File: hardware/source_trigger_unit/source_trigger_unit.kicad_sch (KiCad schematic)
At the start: 12 parts, among them J1 SMA, J2 SMA, J3 BANANA, 4mm, P1 IEC_60320_C13_Plug, SW1 SW_Nidec_CAS-120A1

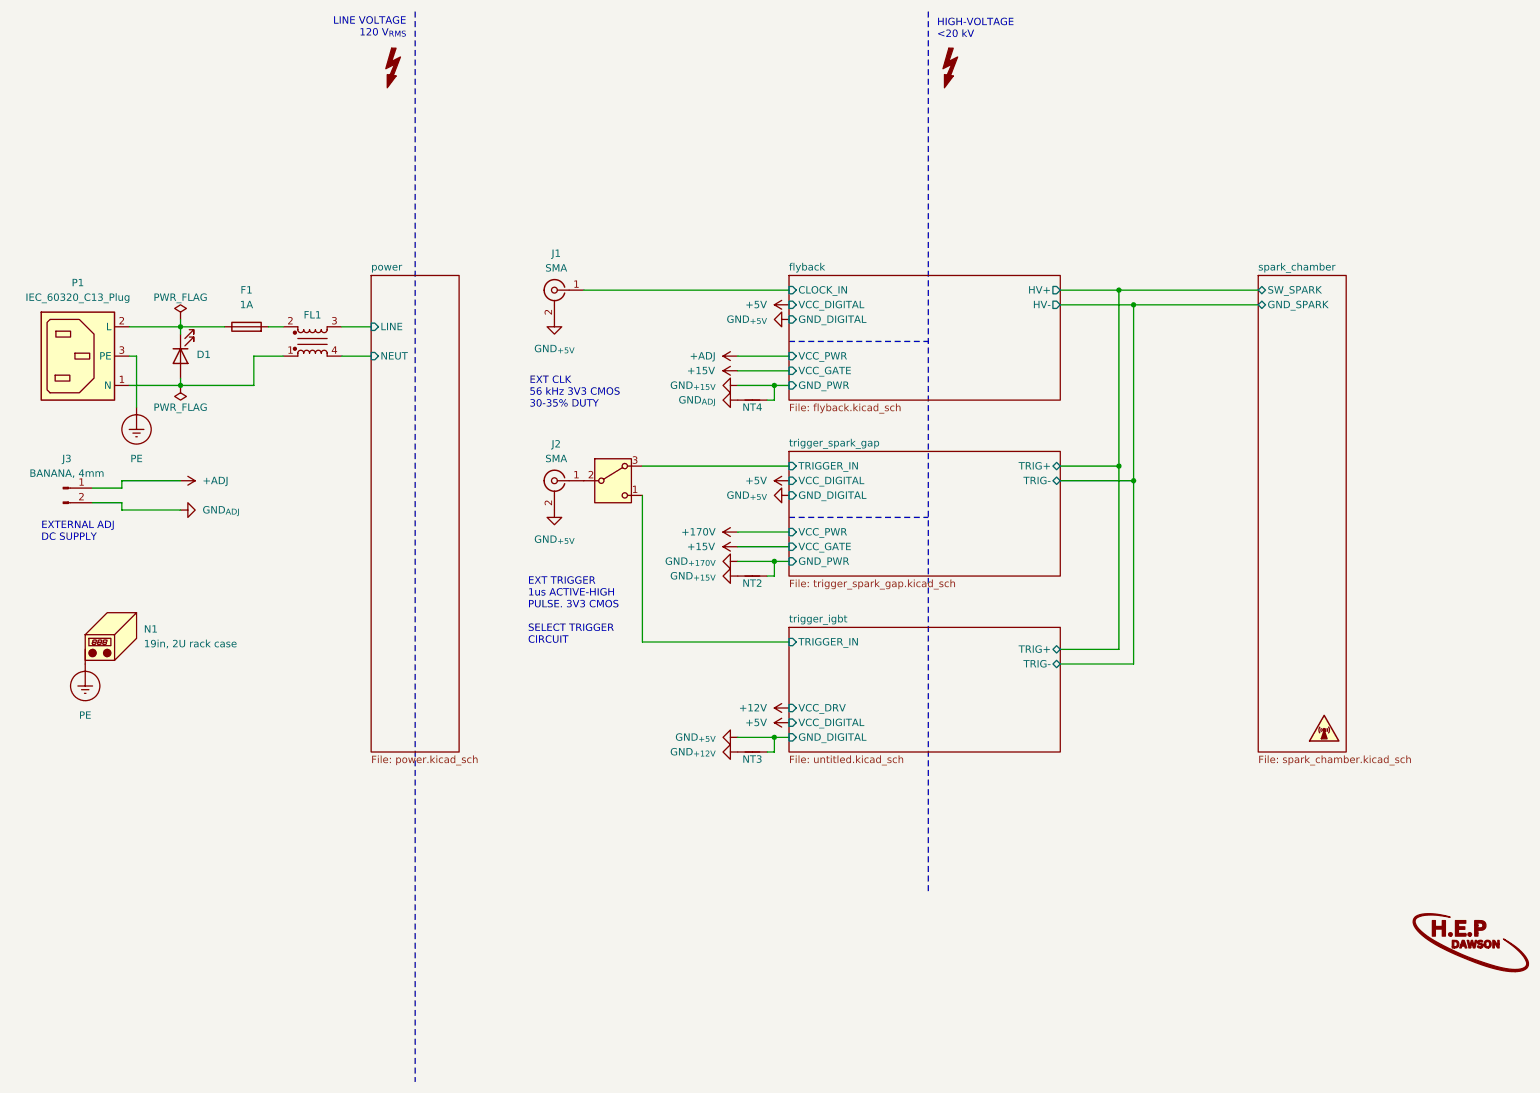
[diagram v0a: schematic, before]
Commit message: add titles & reformat schematics
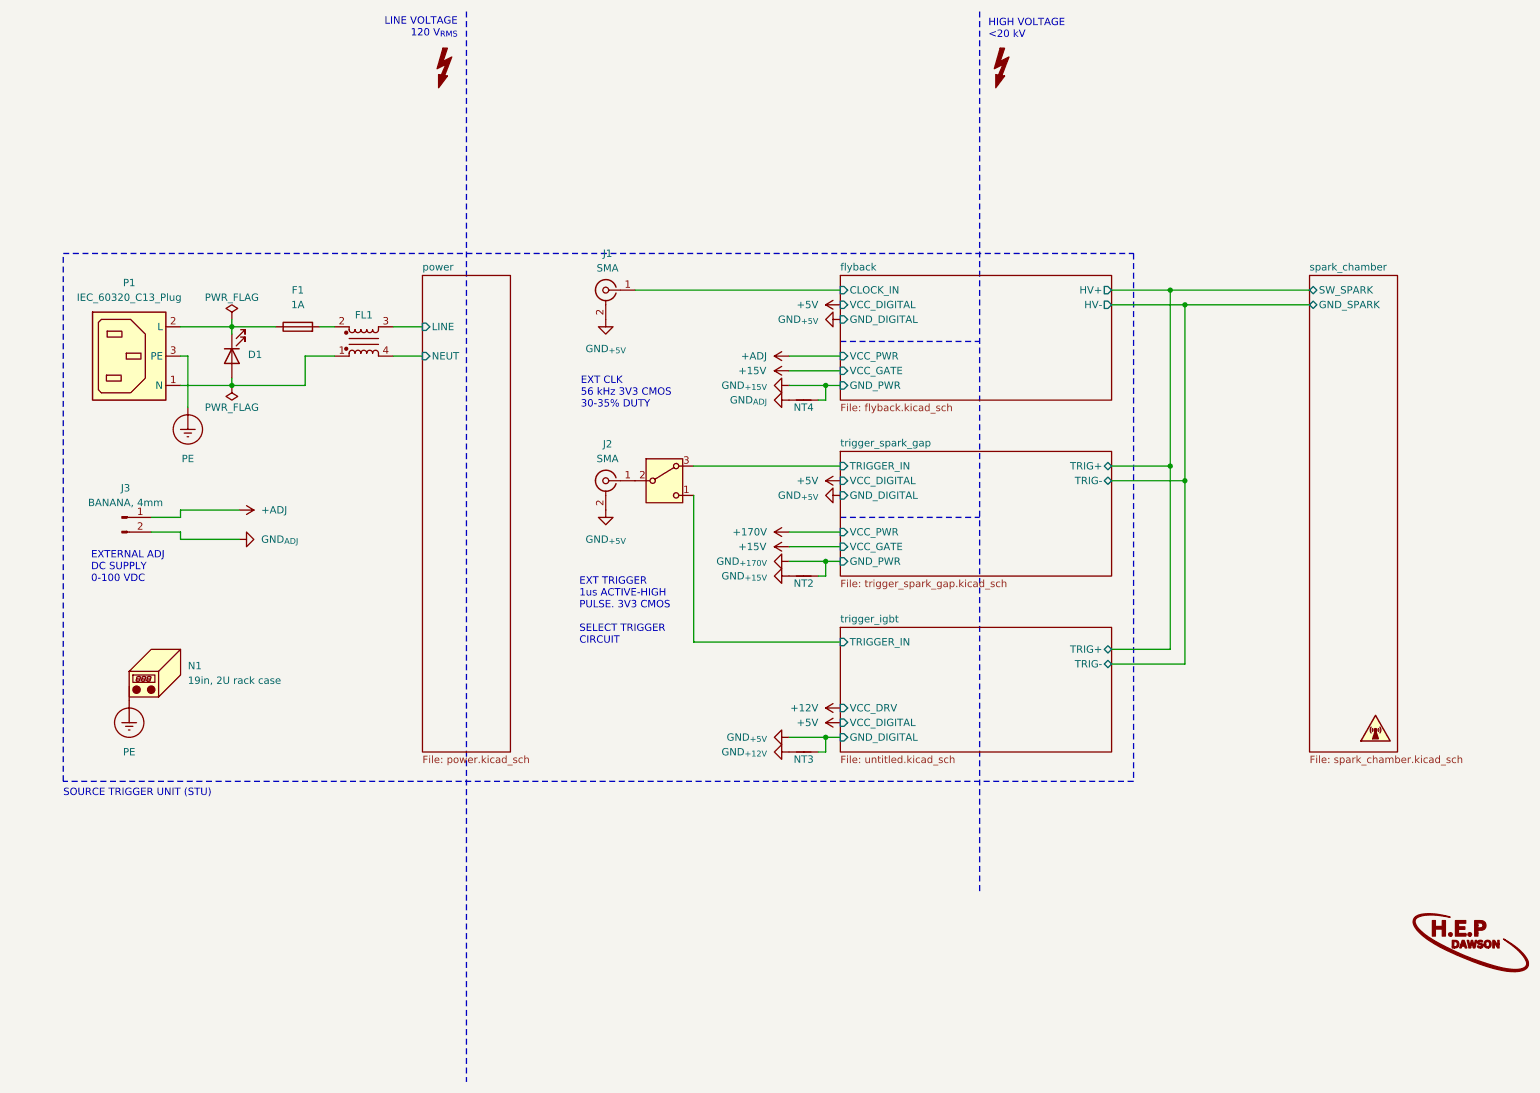
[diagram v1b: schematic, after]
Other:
- note added: "EXTERNAL ADJ DC SUPPLY 0-100 VDC"
- note added: "HIGH VOLTAGE <20 kV"
- note added: "SOURCE TRIGGER UNIT (STU)"
- note removed: "EXTERNAL ADJ DC SUPPLY"
- note removed: "HIGH-VOLTAGE <20 kV"
- title: Source Trigger Unit -> Spark Chamber & Source Trigger Unit (STU)
- moved on the sheet: D1, F1, FL1, J1, J2, J3, N1, NT2, NT3, NT4, P1
